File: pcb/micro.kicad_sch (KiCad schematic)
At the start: 26 parts, among them J2 DBG, SW1 TL3342F160QG/TR, SW2 TL3342F160QG/TR, U1 RP2040, U5 W25Q128JVSIQ, Y1 12MHz

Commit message: First pass of applying footprints to most components.
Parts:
- C10, C11, C12, C13, C14, C15, C16, C17, C4, C5, C6, C7, C8, C9: footprint (none) -> Capacitor_SMD:C_0603_1608Metric_Pad1.08x0.95mm_HandSolder
- J2: footprint (none) -> Connector_PinHeader_2.54mm:PinHeader_1x02_P2.54mm_Horizontal
- R10, R4, R5, R6, R7, R9: footprint (none) -> Resistor_SMD:R_0603_1608Metric_Pad0.98x0.95mm_HandSolder
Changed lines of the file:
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@@
 			)
 		)
-		(property "Footprint" ""
+		(property "Footprint" "Connector_PinHeader_2.54mm:PinHeader_1x02_P2.54mm_Horizontal"
 			(at 109.22 120.65 0)
 			(effects
@@
 			)
 		)
-		(property "Footprint" ""
+		(property "Footprint" "Capacitor_SMD:C_0603_1608Metric_Pad1.08x0.95mm_HandSolder"
 			(at 192.7352 36.83 0)
 			(effects
@@
 			)
 		)
-		(property "Footprint" ""
+		(property "Footprint" "Capacitor_SMD:C_0603_1608Metric_Pad1.08x0.95mm_HandSolder"
 			(at 227.0252 62.23 0)
 			(effects
@@
 			)
 		)
-		(property "Footprint" ""
+		(property "Footprint" "Resistor_SMD:R_0603_1608Metric_Pad0.98x0.95mm_HandSolder"
 			(at 69.85 54.102 90)
 			(effects
@@
 			)
 		)
-		(property "Footprint" ""
+		(property "Footprint" "Capacitor_SMD:C_0603_1608Metric_Pad1.08x0.95mm_HandSolder"
 			(at 199.0852 54.61 0)
 			(effects
@@
 			)
 		)
-		(property "Footprint" ""
+		(property "Footprint" "Capacitor_SMD:C_0603_1608Metric_Pad1.08x0.95mm_HandSolder"
 			(at 211.7852 80.01 0)
 			(effects
@@
 			)
 		)
-		(property "Footprint" ""
+		(property "Footprint" "Resistor_SMD:R_0603_1608Metric_Pad0.98x0.95mm_HandSolder"
 			(at 117.602 50.8 90)
 			(effects
@@
 			)
 		)
-		(property "Footprint" ""
+		(property "Footprint" "Capacitor_SMD:C_0603_1608Metric_Pad1.08x0.95mm_HandSolder"
 			(at 230.8352 36.83 0)
 			(effects
@@
 			)
 		)
-		(property "Footprint" ""
+		(property "Footprint" "Resistor_SMD:R_0603_1608Metric_Pad0.98x0.95mm_HandSolder"
 			(at 69.85 62.992 90)
 			(effects
@@
 			)
 		)
-		(property "Footprint" ""
+		(property "Footprint" "Capacitor_SMD:C_0603_1608Metric_Pad1.08x0.95mm_HandSolder"
 			(at 131.7752 41.91 0)
 			(effects
@@
 			)
 		)
-		(property "Footprint" ""
+		(property "Footprint" "Capacitor_SMD:C_0603_1608Metric_Pad1.08x0.95mm_HandSolder"
 			(at 72.39 95.5548 0)
 			(effects
@@
 			)
 		)
-		(property "Footprint" ""
+		(property "Footprint" "Capacitor_SMD:C_0603_1608Metric_Pad1.08x0.95mm_HandSolder"
 			(at 101.2952 152.4 0)
 			(effects
@@
 			)
 		)
-		(property "Footprint" ""
+		(property "Footprint" "Resistor_SMD:R_0603_1608Metric_Pad0.98x0.95mm_HandSolder"
 			(at 59.69 149.098 90)
 			(effects
@@
 			)
 		)
-		(property "Footprint" ""
+		(property "Footprint" "Capacitor_SMD:C_0603_1608Metric_Pad1.08x0.95mm_HandSolder"
 			(at 72.39 112.0648 0)
 			(effects
@@
 			)
 		)
-		(property "Footprint" ""
+		(property "Footprint" "Capacitor_SMD:C_0603_1608Metric_Pad1.08x0.95mm_HandSolder"
 			(at 243.5352 36.83 0)
 			(effects
@@
 			)
 		)
-		(property "Footprint" ""
+		(property "Footprint" "Resistor_SMD:R_0603_1608Metric_Pad0.98x0.95mm_HandSolder"
 			(at 70.612 148.59 90)
 			(effects
@@
 			)
 		)
-		(property "Footprint" ""
+		(property "Footprint" "Capacitor_SMD:C_0603_1608Metric_Pad1.08x0.95mm_HandSolder"
 			(at 224.4852 80.01 0)
 			(effects
@@
 			)
 		)
-		(property "Footprint" ""
+		(property "Footprint" "Capacitor_SMD:C_0603_1608Metric_Pad1.08x0.95mm_HandSolder"
 			(at 180.0352 36.83 0)
 			(effects
@@
 			)
 		)
-		(property "Footprint" ""
+		(property "Footprint" "Resistor_SMD:R_0603_1608Metric_Pad0.98x0.95mm_HandSolder"
 			(at 115.57 112.268 90)
 			(effects
@@
 			)
 		)
-		(property "Footprint" ""
+		(property "Footprint" "Capacitor_SMD:C_0603_1608Metric_Pad1.08x0.95mm_HandSolder"
 			(at 218.1352 36.83 0)
 			(effects
@@
 			)
 		)
-		(property "Footprint" ""
+		(property "Footprint" "Capacitor_SMD:C_0603_1608Metric_Pad1.08x0.95mm_HandSolder"
 			(at 205.4352 36.83 0)
 			(effects

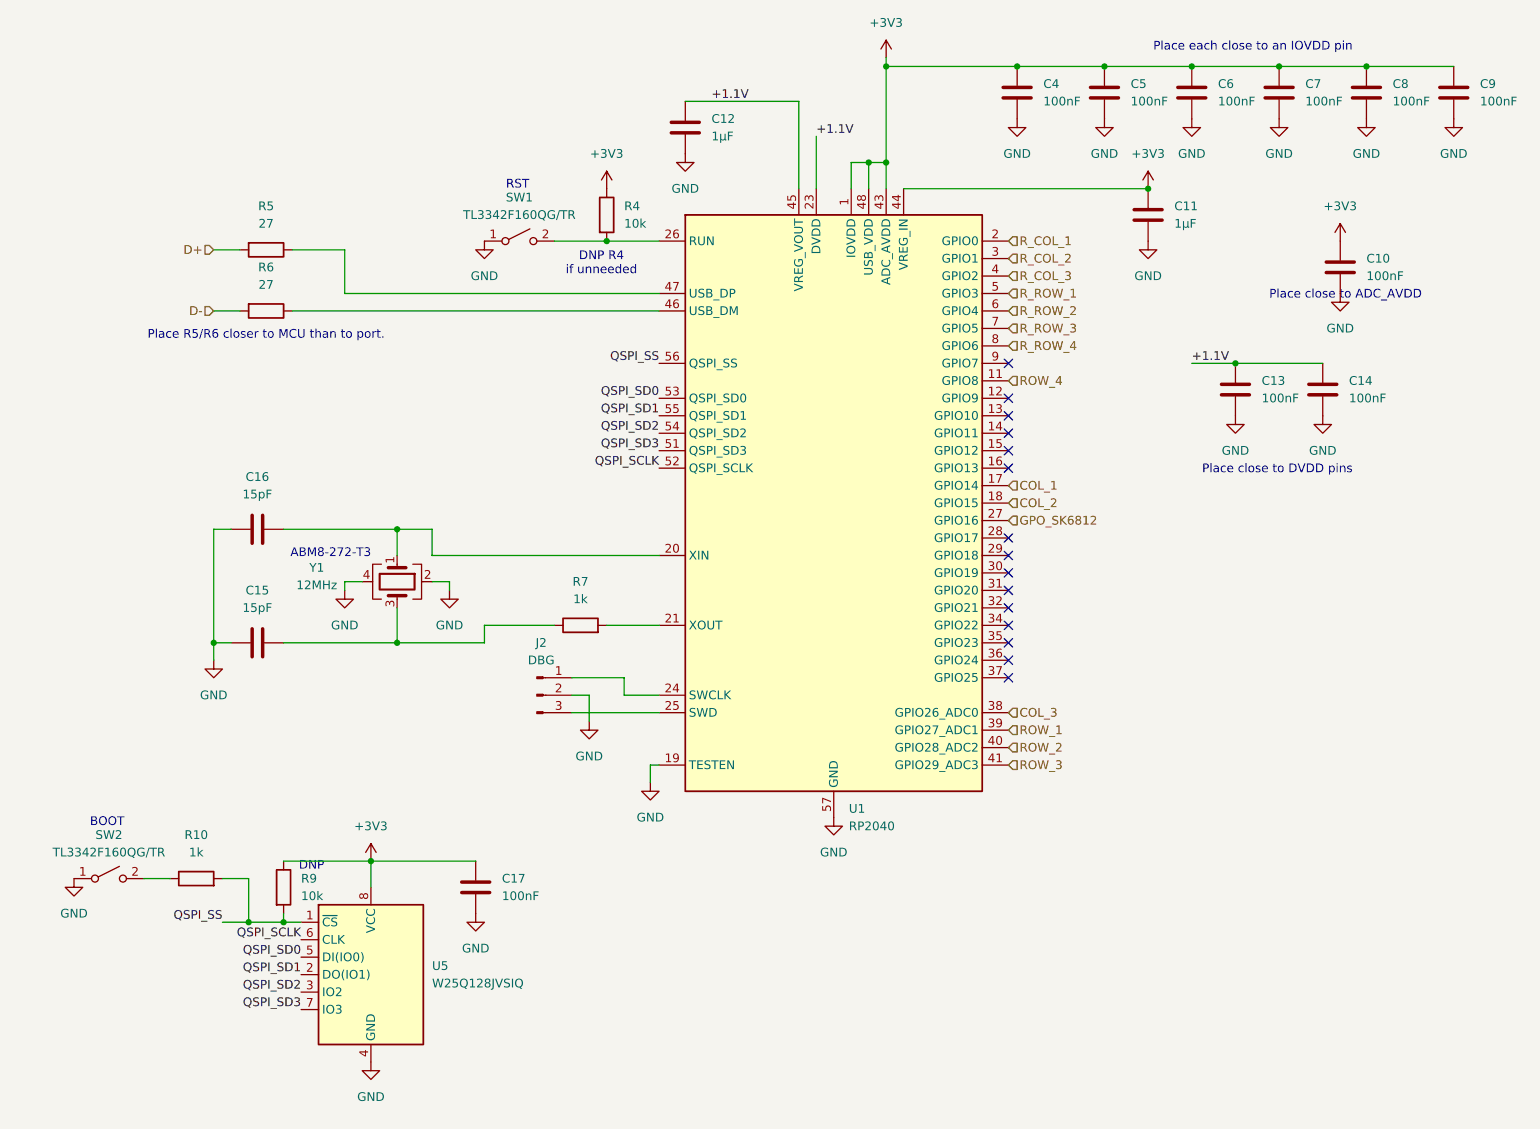
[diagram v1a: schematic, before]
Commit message: Switching from a full USB protection chip for OVP and ESD, needed for USB PD to only ESD protection. Also added chips for ESD protection for the Ethernet connectors to the other hand.
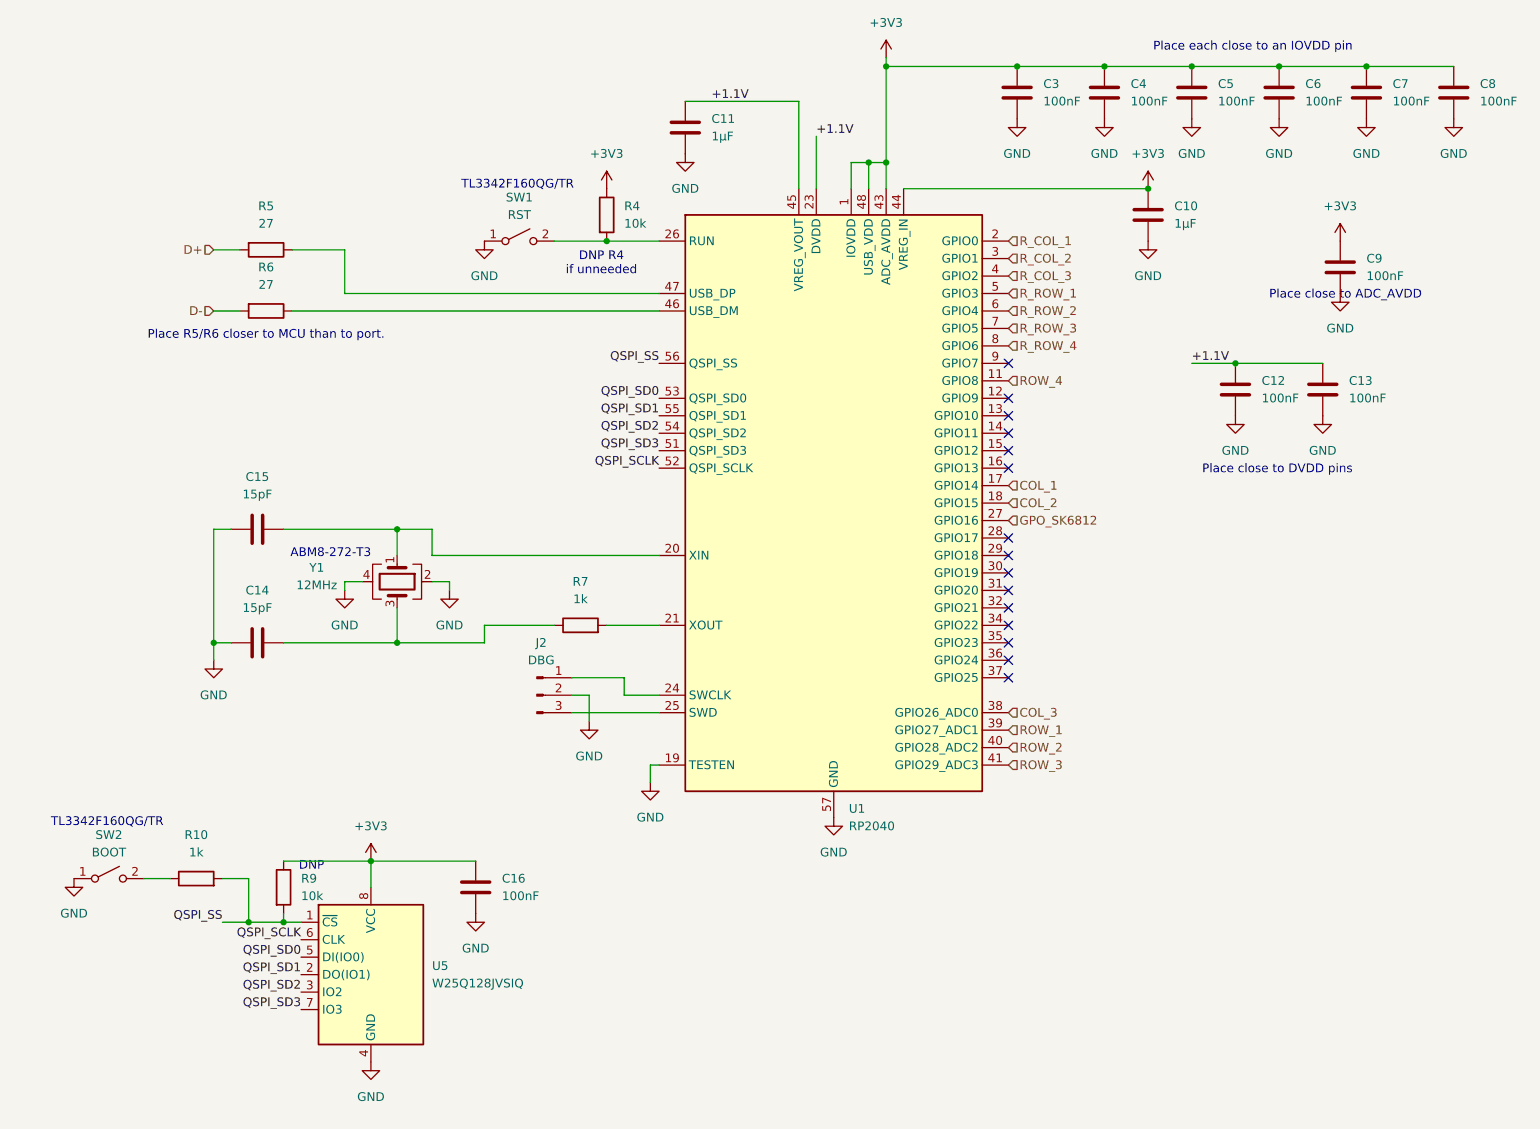
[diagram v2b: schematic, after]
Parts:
- SW1: value TL3342F160QG/TR -> RST
- SW2: value TL3342F160QG/TR -> BOOT
- renumbered C11 to C10, C12 to C11, C13 to C12, C14 to C13, C15 to C14, C16 to C15, C17 to C16, C4 to C3, C5 to C4, C6 to C5, C7 to C6, C8 to C7, C9 to C8, C10 to C9
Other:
- note added: "TL3342F160QG/TR"
- note removed: "BOOT"
- note removed: "RST"
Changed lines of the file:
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@@
 		)
 	)
-	(text "RST"
+	(text "TL3342F160QG/TR"
 		(exclude_from_sim no)
 		(at 106.426 46.482 0)
@@
 		)
 	)
-	(text "BOOT"
+	(text "TL3342F160QG/TR"
 		(exclude_from_sim no)
 		(at 46.736 139.192 0)
@@
 		(dnp no)
 		(fields_autoplaced yes)
-		(property "Reference" "C5"
+		(property "Reference" "C4"
 			(at 195.58 31.7499 0)
 			(effects
@@
 			(project "cheapino"
 				(path "/9203b006-47ac-4f34-8cc4-2b709e3df56f/b2f85b86-5933-4a5f-88c2-315afb4ca3cd"
-					(reference "C5")
+					(reference "C4")
 					(unit 1)
 				)
@@
 		(dnp no)
 		(fields_autoplaced yes)
-		(property "Reference" "C10"
+		(property "Reference" "C9"
 			(at 229.87 57.1499 0)
 			(effects
@@
 			(project "cheapino"
 				(path "/9203b006-47ac-4f34-8cc4-2b709e3df56f/b2f85b86-5933-4a5f-88c2-315afb4ca3cd"
-					(reference "C10")
+					(reference "C9")
 					(unit 1)
 				)
@@
 		(dnp no)
 		(fields_autoplaced yes)
-		(property "Reference" "C11"
+		(property "Reference" "C10"
 			(at 201.93 49.5299 0)
 			(effects
@@
 			(project "cheapino"
 				(path "/9203b006-47ac-4f34-8cc4-2b709e3df56f/b2f85b86-5933-4a5f-88c2-315afb4ca3cd"
-					(reference "C11")
+					(reference "C10")
 					(unit 1)
 				)
@@
 		(dnp no)
 		(fields_autoplaced yes)
-		(property "Reference" "C13"
+		(property "Reference" "C12"
 			(at 214.63 74.9299 0)
 			(effects
@@
 			(project "cheapino"
 				(path "/9203b006-47ac-4f34-8cc4-2b709e3df56f/b2f85b86-5933-4a5f-88c2-315afb4ca3cd"
-					(reference "C13")
+					(reference "C12")
 					(unit 1)
 				)
@@
 		(dnp no)
 		(fields_autoplaced yes)
-		(property "Reference" "C8"
+		(property "Reference" "C7"
 			(at 233.68 31.7499 0)
 			(effects
@@
 			(project "cheapino"
 				(path "/9203b006-47ac-4f34-8cc4-2b709e3df56f/b2f85b86-5933-4a5f-88c2-315afb4ca3cd"
-					(reference "C8")
+					(reference "C7")
 					(unit 1)
 				)
@@
 		(dnp no)
 		(fields_autoplaced yes)
-		(property "Reference" "C12"
+		(property "Reference" "C11"
 			(at 134.62 36.8299 0)
 			(effects
@@
 			(project "cheapino"
 				(path "/9203b006-47ac-4f34-8cc4-2b709e3df56f/b2f85b86-5933-4a5f-88c2-315afb4ca3cd"
-					(reference "C12")
+					(reference "C11")
 					(unit 1)
 				)
@@
 			)
 		)
-		(property "Value" "TL3342F160QG/TR"
+		(property "Value" "RST"
 			(at 106.68 50.8 0)
 			(effects
@@
 		(dnp no)
 		(fields_autoplaced yes)
-		(property "Reference" "C16"
+		(property "Reference" "C15"
 			(at 68.58 88.9 90)
 			(effects
@@
 			(project "cheapino"
 				(path "/9203b006-47ac-4f34-8cc4-2b709e3df56f/b2f85b86-5933-4a5f-88c2-315afb4ca3cd"
-					(reference "C16")
+					(reference "C15")
 					(unit 1)
 				)
@@
 		(dnp no)
 		(fields_autoplaced yes)
-		(property "Reference" "C17"
+		(property "Reference" "C16"
 			(at 104.14 147.3199 0)
 			(effects
@@
 			(project "cheapino"
 				(path "/9203b006-47ac-4f34-8cc4-2b709e3df56f/b2f85b86-5933-4a5f-88c2-315afb4ca3cd"
-					(reference "C17")
+					(reference "C16")
 					(unit 1)
 				)
@@
 		(dnp no)
 		(fields_autoplaced yes)
-		(property "Reference" "C15"
+		(property "Reference" "C14"
 			(at 68.58 105.41 90)
 			(effects
@@
 			(project ""
 				(path "/9203b006-47ac-4f34-8cc4-2b709e3df56f/b2f85b86-5933-4a5f-88c2-315afb4ca3cd"
-					(reference "C15")
+					(reference "C14")
 					(unit 1)
 				)
@@
 		(dnp no)
 		(fields_autoplaced yes)
-		(property "Reference" "C9"
+		(property "Reference" "C8"
 			(at 246.38 31.7499 0)
 			(effects
@@
 			(project "cheapino"
 				(path "/9203b006-47ac-4f34-8cc4-2b709e3df56f/b2f85b86-5933-4a5f-88c2-315afb4ca3cd"
-					(reference "C9")
+					(reference "C8")
 					(unit 1)
 				)
@@
 		(dnp no)
 		(fields_autoplaced yes)
-		(property "Reference" "C14"
+		(property "Reference" "C13"
 			(at 227.33 74.9299 0)
 			(effects
@@
 			(project "cheapino"
 				(path "/9203b006-47ac-4f34-8cc4-2b709e3df56f/b2f85b86-5933-4a5f-88c2-315afb4ca3cd"
-					(reference "C14")
+					(reference "C13")
 					(unit 1)
 				)
@@
 		(dnp no)
 		(fields_autoplaced yes)
-		(property "Reference" "C4"
+		(property "Reference" "C3"
 			(at 182.88 31.7499 0)
 			(effects
@@
 			(project ""
 				(path "/9203b006-47ac-4f34-8cc4-2b709e3df56f/b2f85b86-5933-4a5f-88c2-315afb4ca3cd"
-					(reference "C4")
+					(reference "C3")
 					(unit 1)
 				)
@@
 			)
 		)
-		(property "Value" "TL3342F160QG/TR"
+		(property "Value" "BOOT"
 			(at 46.99 143.51 0)
 			(effects
@@
 		(dnp no)
 		(fields_autoplaced yes)
-		(property "Reference" "C7"
+		(property "Reference" "C6"
 			(at 220.98 31.7499 0)
 			(effects
@@
 			(project "cheapino"
 				(path "/9203b006-47ac-4f34-8cc4-2b709e3df56f/b2f85b86-5933-4a5f-88c2-315afb4ca3cd"
-					(reference "C7")
+					(reference "C6")
 					(unit 1)
 				)
@@
 		(dnp no)
 		(fields_autoplaced yes)
-		(property "Reference" "C6"
+		(property "Reference" "C5"
 			(at 208.28 31.7499 0)
 			(effects
@@
 			(project "cheapino"
 				(path "/9203b006-47ac-4f34-8cc4-2b709e3df56f/b2f85b86-5933-4a5f-88c2-315afb4ca3cd"
-					(reference "C6")
+					(reference "C5")
 					(unit 1)
 				)

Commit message: Updated all footprints and libraries to match planned components.
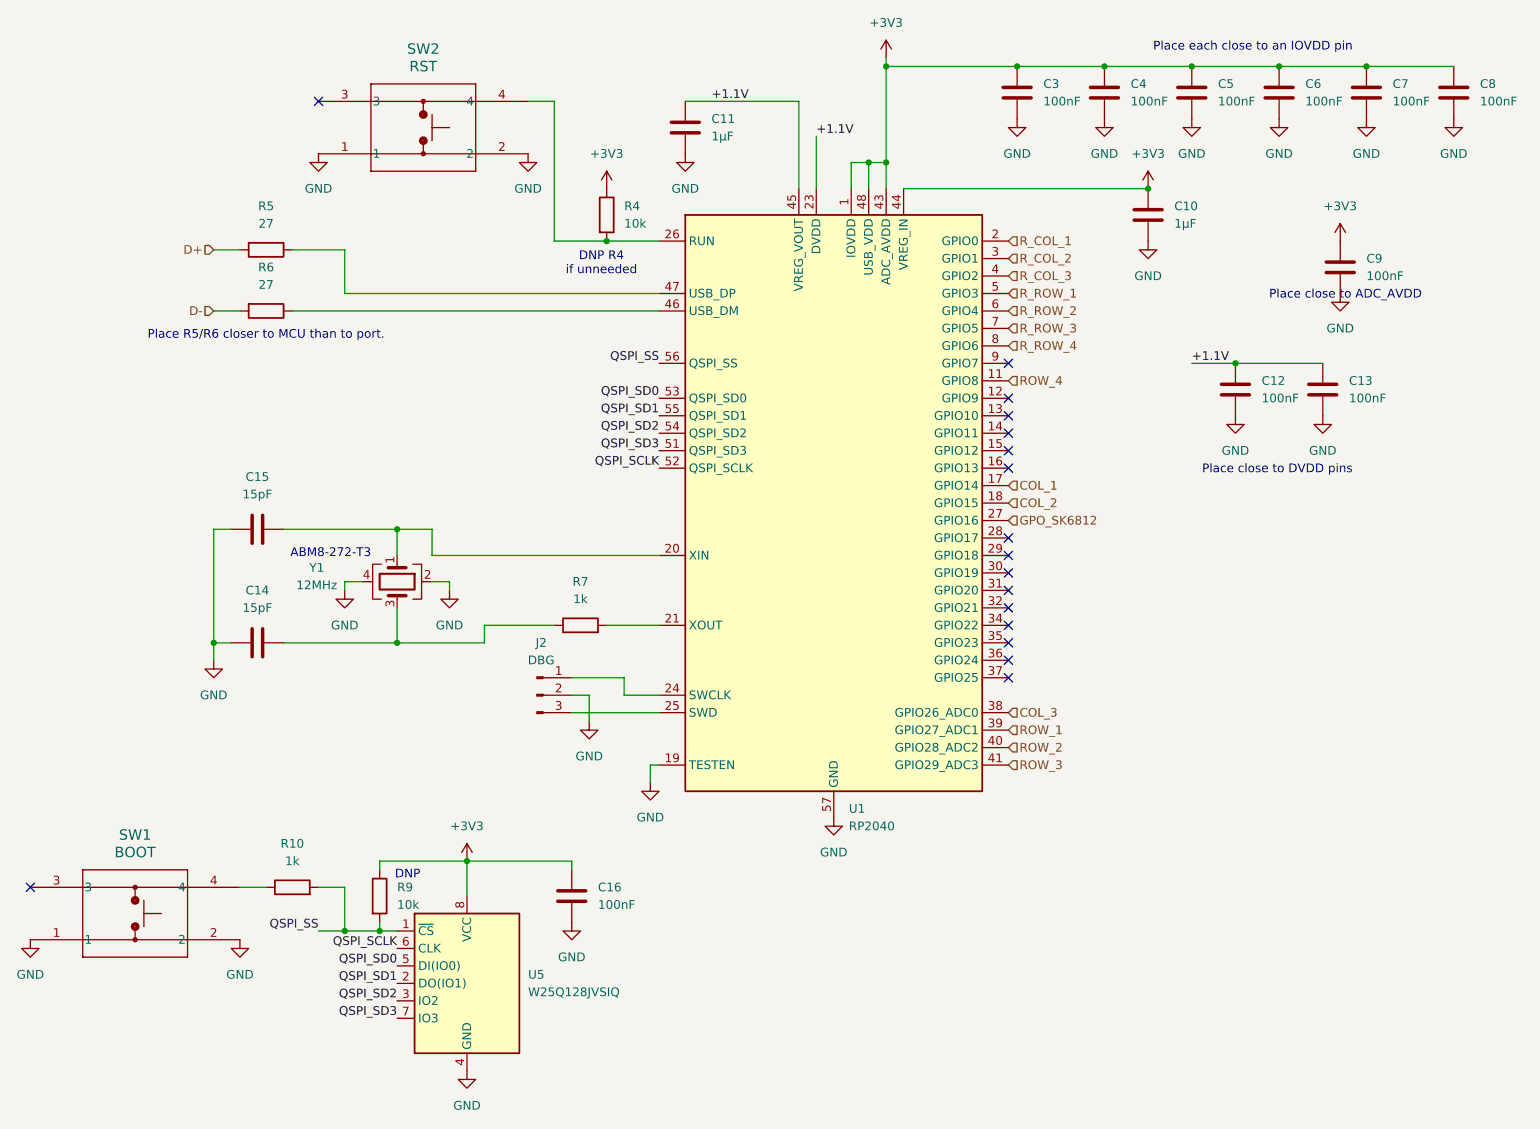
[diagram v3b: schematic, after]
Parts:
- removed SW1: RST, symbol Switch:SW_SPST
- removed SW2: BOOT, symbol Switch:SW_SPST
- added SW1: BOOT, Extra:TL3342_EWI, symbol Extra:TL3342F160QG
- added SW2: RST, Extra:TL3342_EWI, symbol Extra:TL3342F160QG
- Y1: footprint (none) -> Extra:ABM8272T3
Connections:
- net GND: now also SW1.1, SW1.2, SW2.1, SW2.2
- net at R4.2, U1.26 (RUN): now also SW2.4
- net at R10.1: now also SW1.4
- no-connect marks 15 -> 17
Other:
- note removed: "TL3342F160QG/TR"
- moved on the sheet: C16, R10, R9, U5

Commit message: Removed Rotary Encoder for space/flippability reasons and replaced all the key switch footprints that weren't bound properly to the schematic for some reason.
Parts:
- J2: footprint Connector_PinHeader_2.54mm:PinHeader_1x02_P2.54mm_Horizontal -> Connector_PinHeader_2.54mm:PinHeader_1x03_P2.54mm_Vertical
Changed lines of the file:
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@@
 			)
 		)
-		(property "Footprint" "Connector_PinHeader_2.54mm:PinHeader_1x02_P2.54mm_Horizontal"
+		(property "Footprint" "Connector_PinHeader_2.54mm:PinHeader_1x03_P2.54mm_Vertical"
 			(at 109.22 120.65 0)
 			(effects
